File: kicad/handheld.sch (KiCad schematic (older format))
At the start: 23 parts, among them J1 Conn_01x08, J2 61300311121, J3 AVR-PDI-6, SW1 HOLD, SW2 PAUSE, SW3 SDROP, SW4 HDROP, SW5 ROTR, SW6 RIGHT, SW7 ROTL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

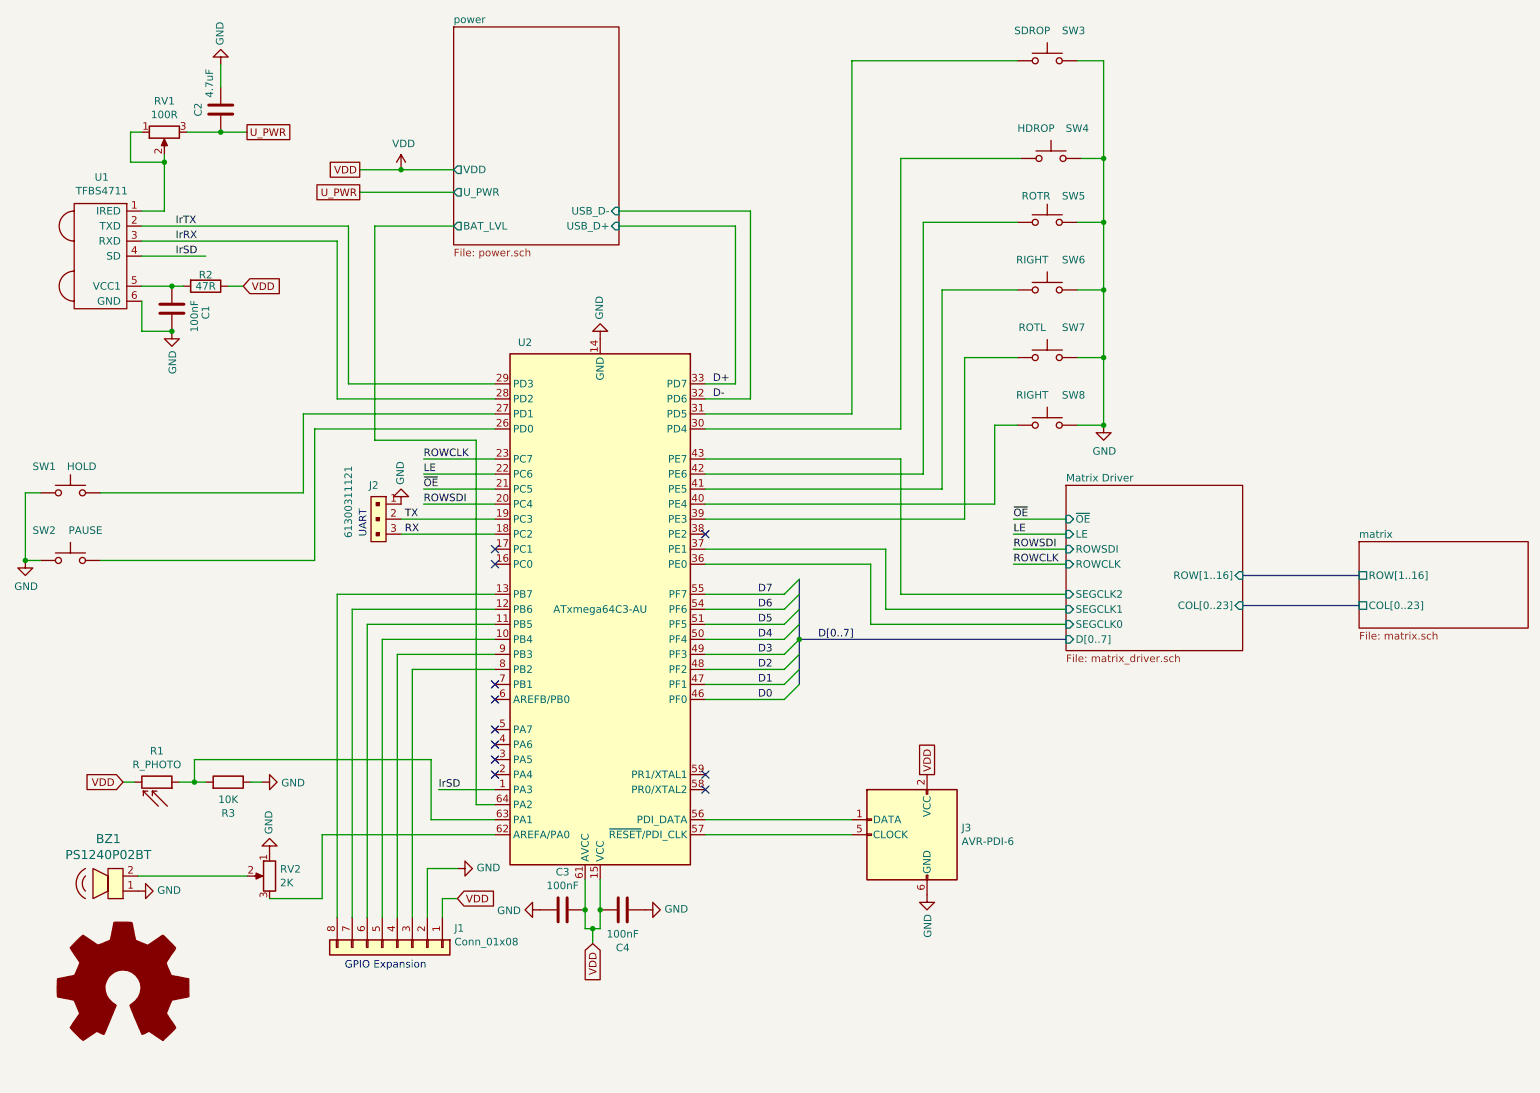
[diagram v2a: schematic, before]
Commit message: Decouple microcontroller
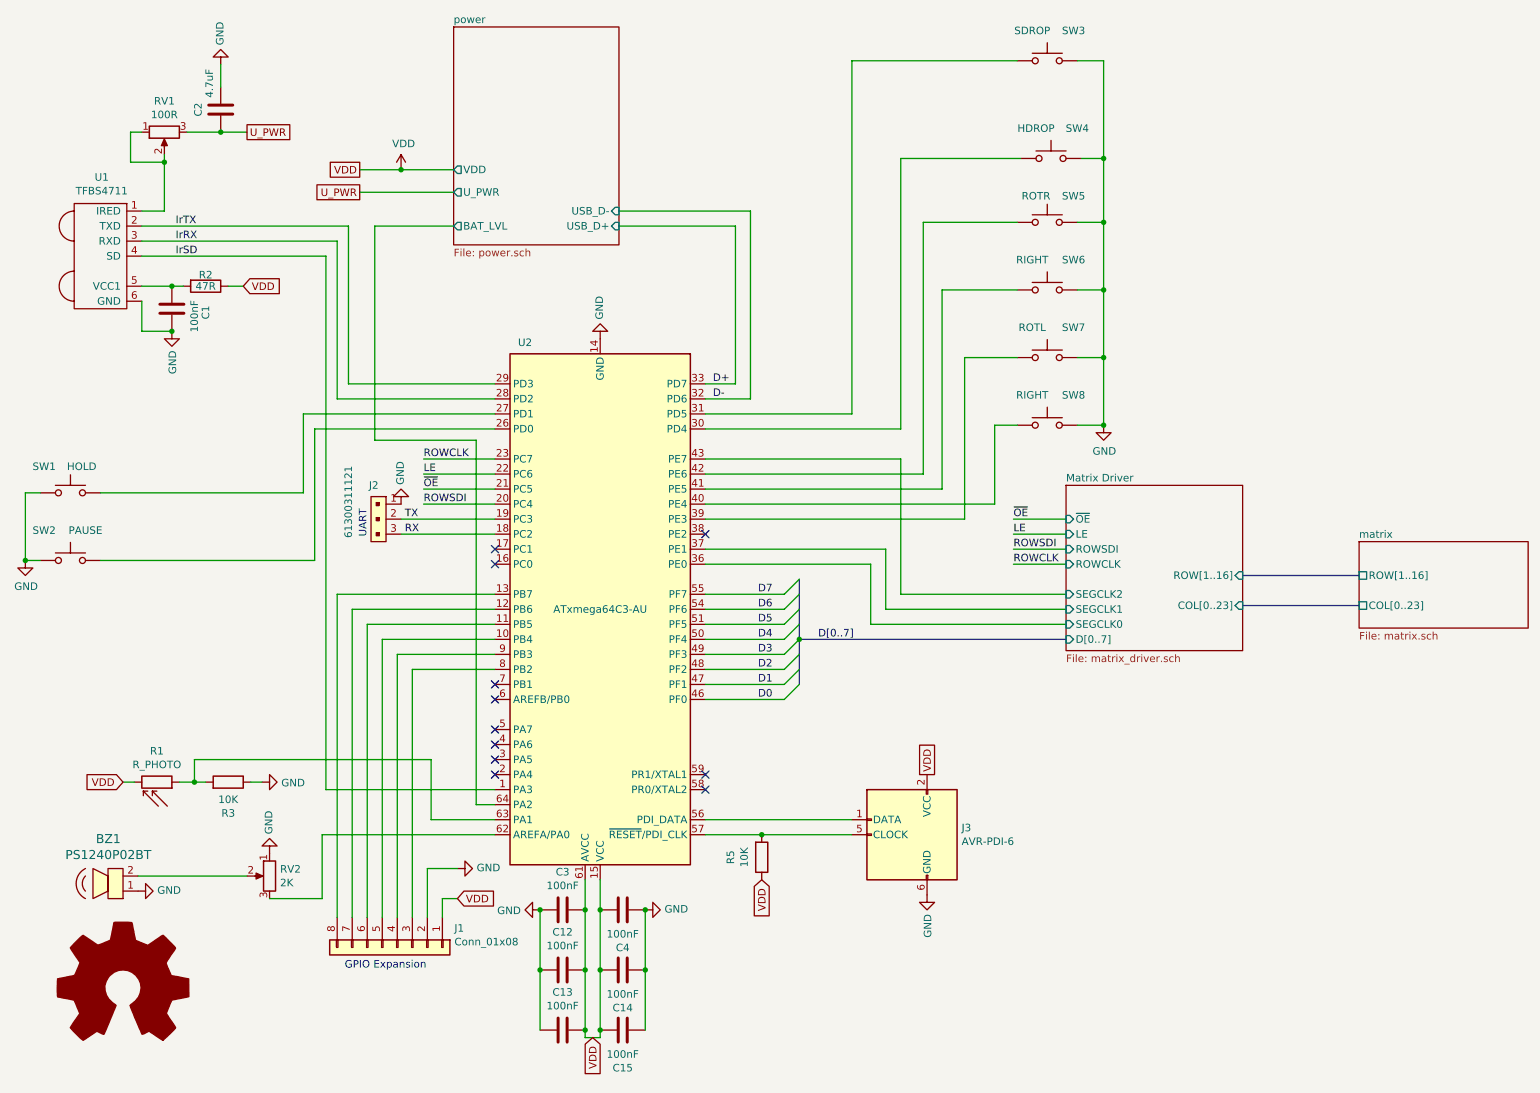
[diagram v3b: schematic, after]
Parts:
- added C12, C13, C14, C15: 100nF, Capacitor_SMD:C_0805_2012Metric_Pad1.15x1.40mm_HandSolder, symbol Device:C
- added R5: 10K, Resistor_SMD:R_0805_2012Metric_Pad1.15x1.40mm_HandSolder, symbol Device:R
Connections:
- net GND: now also C12.2, C13.2, C14.2, C15.2
- net VDD: now also C12.1, C13.1, C14.1, C15.1, R5.1
- net at J3.5 (CLOCK), U2.57 (~RESET~/PDI_CLK): now also R5.2
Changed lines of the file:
@@
 	4350 6475 4350 6675
 Wire Wire Line
-	4350 6675 4350 6800
-Wire Wire Line
-	4450 6800 4450 6675
-Connection ~ 4350 6675
-Connection ~ 4450 6675
+	4450 7525 4450 7475
 $Comp
 L Connector:AVR-PDI-6 J3
@@
 $EndComp
 Wire Wire Line
-	6125 6175 5150 6175
+	6125 6175 5525 6175
 Wire Wire Line
 	5150 6075 6125 6075
@@
 Wire Wire Line
 	3125 1750 3475 1750
-Text GLabel 4400 6900 3    50   Input ~ 0
+Text GLabel 4400 7525 3    50   Input ~ 0
 VDD
-Wire Wire Line
-	4350 6800 4400 6800
-Wire Wire Line
-	4400 6800 4400 6900
-Connection ~ 4400 6800
-Wire Wire Line
-	4400 6800 4450 6800
 Text GLabel 6625 5775 1    50   UnSpc ~ 0
 VDD
@@
 Wire Wire Line
 	2775 3175 3750 3175
-Wire Wire Line
-	3750 5875 3375 5875
-Text Label 3375 5875 0    50   ~ 0
-IrSD
 Text Label 1625 2325 0    50   ~ 0
 IrSD
-Wire Wire Line
-	1400 2325 1825 2325
 NoConn ~ 3750 4375
 NoConn ~ 3750 5475
@@
 	3200 5075 3200 6725
 NoConn ~ 3750 5175
+Wire Wire Line
+	4350 6675 4350 7075
+Connection ~ 4350 6675
+Connection ~ 4450 6675
+$Comp
+L Device:C C12
+U 1 1 5FD69EC0
+P 4200 7075
+F 0 "C12" V 3948 7075 50  0000 C CNN
+F 1 "100nF" V 4039 7075 50  0000 C CNN
+F 2 "Capacitor_SMD:C_0805_2012Metric_Pad1.15x1.40mm_HandSolder" H 4238 6925 50  0001 C CNN
+F 3 "~" H 4200 7075 50  0001 C CNN
+	1    4200 7075
+	0    1    1    0
+$EndComp
+Connection ~ 4350 7075
+Wire Wire Line
+	4350 7075 4350 7475
+$Comp
+L Device:C C14
+U 1 1 5FD6AC2B
+P 4600 7075
+F 0 "C14" V 4348 7075 50  0000 C CNN
+F 1 "100nF" V 4439 7075 50  0000 C CNN
+F 2 "Capacitor_SMD:C_0805_2012Metric_Pad1.15x1.40mm_HandSolder" H 4638 6925 50  0001 C CNN
+F 3 "~" H 4600 7075 50  0001 C CNN
+	1    4600 7075
+	0    -1   -1   0
+$EndComp
+Connection ~ 4450 7075
+Wire Wire Line
+	4450 7075 4450 6675
+$Comp
+L Device:C C13
+U 1 1 5FD6B34C
+P 4200 7475
+F 0 "C13" V 3948 7475 50  0000 C CNN
+F 1 "100nF" V 4039 7475 50  0000 C CNN
+F 2 "Capacitor_SMD:C_0805_2012Metric_Pad1.15x1.40mm_HandSolder" H 4238 7325 50  0001 C CNN
+F 3 "~" H 4200 7475 50  0001 C CNN
+	1    4200 7475
+	0    1    1    0
+$EndComp
+Connection ~ 4350 7475
+Wire Wire Line
+	4350 7475 4350 7525
+Wire Wire Line
+	4050 7475 4050 7075
+Connection ~ 4050 6675
+Connection ~ 4050 7075
+Wire Wire Line
+	4050 7075 4050 6675
+Wire Wire Line
+	4750 7075 4750 6675
+Connection ~ 4750 6675
+$Comp
+L Device:R R5
+U 1 1 5FD78AC8
+P 5525 6325
+F 0 "R5" V 5318 6325 50  0000 C CNN
+F 1 "10K" V 5409 6325 50  0000 C CNN
+F 2 "Resistor_SMD:R_0805_2012Metric_Pad1.15x1.40mm_HandSolder" V 5455 6325 50  0001 C CNN
+F 3 "~" H 5525 6325 50  0001 C CNN
+	1    5525 6325
+	1    0    0    1
+$EndComp
+Connection ~ 5525 6175
+Wire Wire Line
+	5525 6175 5150 6175
+Text GLabel 5525 6475 3    50   Input ~ 0
+VDD
+Wire Wire Line
+	4350 7525 4450 7525
+$Comp
+L Device:C C15
+U 1 1 5FDA21B7
+P 4600 7475
+F 0 "C15" V 4348 7475 50  0000 C CNN
+F 1 "100nF" V 4439 7475 50  0000 C CNN
+F 2 "Capacitor_SMD:C_0805_2012Metric_Pad1.15x1.40mm_HandSolder" H 4638 7325 50  0001 C CNN
+F 3 "~" H 4600 7475 50  0001 C CNN
+	1    4600 7475
+	0    -1   -1   0
+$EndComp
+Connection ~ 4450 7475
+Wire Wire Line
+	4450 7475 4450 7075
+Wire Wire Line
+	4750 7075 4750 7475
+Connection ~ 4750 7075
+Wire Wire Line
+	2625 2325 2625 5875
+Wire Wire Line
+	2625 5875 3750 5875
+Wire Wire Line
+	1400 2325 2625 2325
 Wire Bus Line
 	5775 4875 5775 5175

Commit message: Adds SELECT button
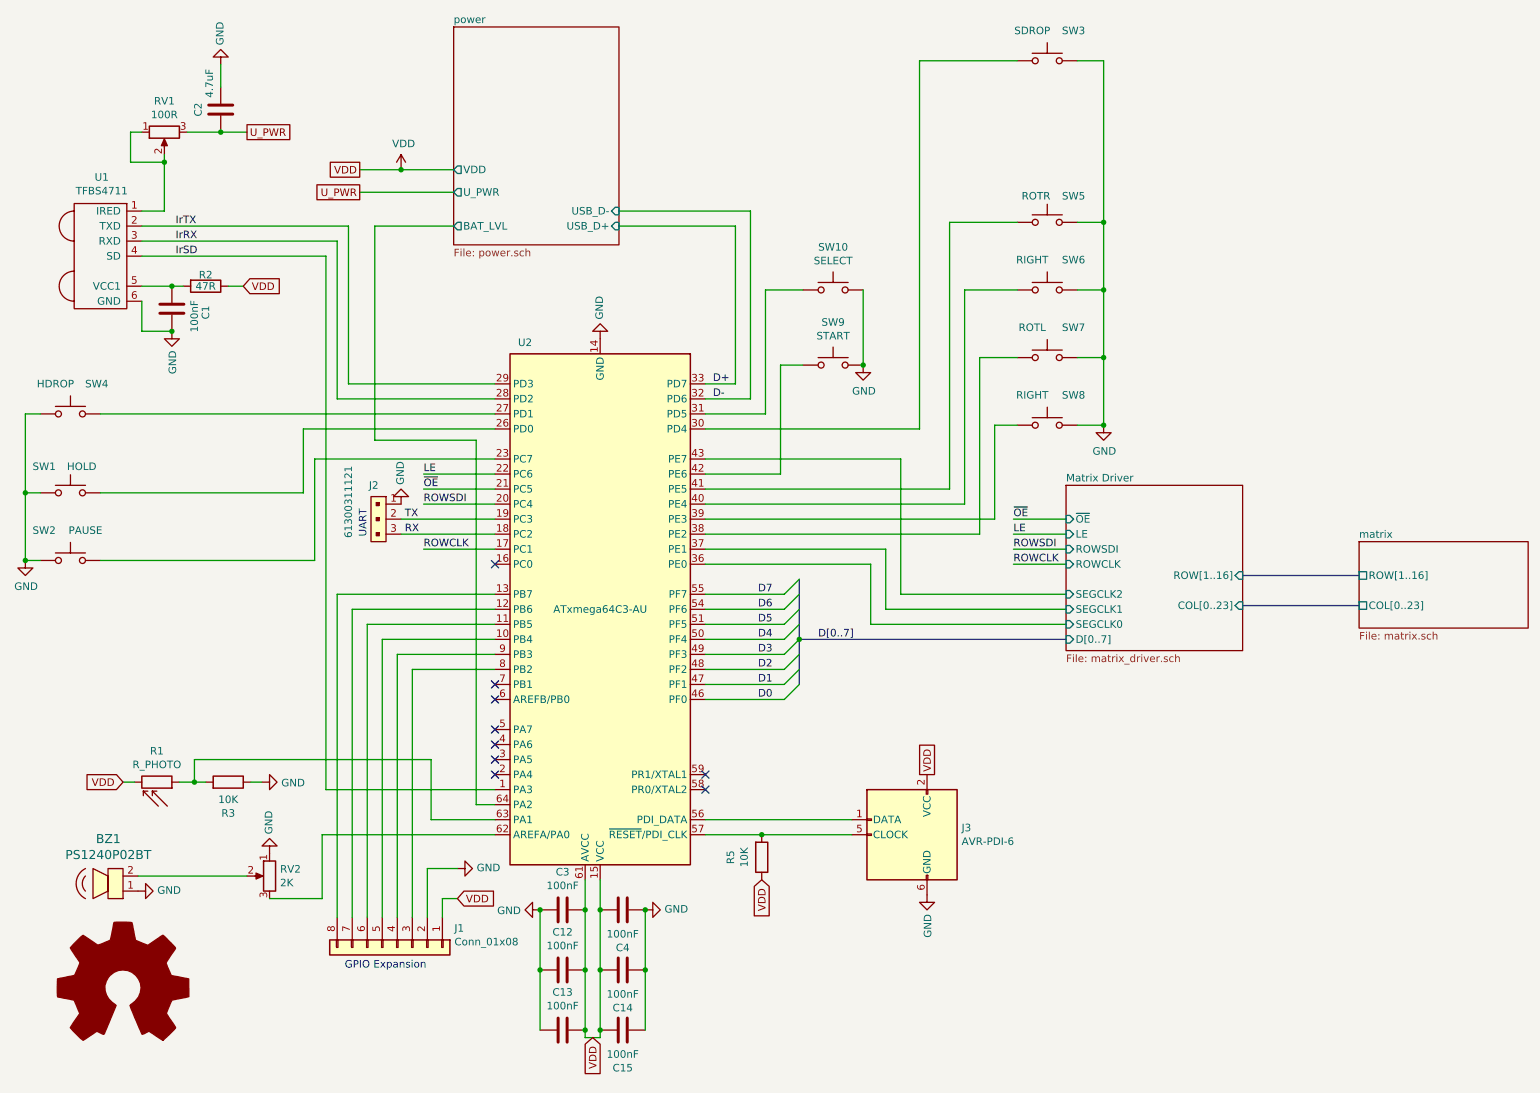
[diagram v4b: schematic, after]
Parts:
- added SW10: SELECT, Button_Switch_THT:SW_PUSH_6mm, symbol Switch:SW_Push
- added SW9: START, Button_Switch_THT:SW_PUSH_6mm, symbol Switch:SW_Push
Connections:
- net GND: now also SW4.2, SW10.2, SW9.2; no longer SW4.1
- net ROWCLK: now also U2.17 (PC1); no longer U2.23 (PC7)
- net at U2.30 (PD4): now also SW3.2; no longer SW4.2
- net at U2.31 (PD5): now also SW10.1; no longer SW3.2
- net at SW2.2: now also U2.23 (PC7); no longer U2.26 (PD0)
- net at U2.27 (PD1): now also SW4.1; no longer SW1.2
- net at SW8.2: now also U2.39 (PE3); no longer U2.40 (PE4)
- net at SW7.2: now also U2.38 (PE2); no longer U2.39 (PE3)
- net at SW6.2: now also U2.40 (PE4); no longer U2.41 (PE5)
- net at SW5.2: now also U2.41 (PE5); no longer U2.42 (PE6)
- new net: SW1.2, U2.26 (PD0)
- new net: SW9.1, U2.42 (PE6)
- no-connect marks 11 -> 9
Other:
- moved on the sheet: SW4
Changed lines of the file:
@@
 Wire Wire Line
 	1925 1500 2100 1500
-NoConn ~ 3750 4275
 Wire Wire Line
 	3625 3550 3625 5975
@@
 	3275 3875 3750 3875
 Wire Wire Line
-	3275 3675 3750 3675
+	3275 4275 3750 4275
 Wire Wire Line
 	3275 3775 3750 3775
@@
 L Switch:SW_Push SW4
 U 1 1 5FBDC4D1
-P 7450 1675
-F 0 "SW4" H 7275 1875 50  0000 C CNN
-F 1 "HDROP" H 7550 1875 50  0000 C CNN
-F 2 "Button_Switch_THT:SW_PUSH-12mm" H 7450 1875 50  0001 C CNN
-F 3 "~" H 7450 1875 50  0001 C CNN
-	1    7450 1675
+P 925 3375
+F 0 "SW4" H 750 3575 50  0000 C CNN
+F 1 "HDROP" H 1025 3575 50  0000 C CNN
+F 2 "Button_Switch_THT:SW_PUSH-12mm" H 925 3575 50  0001 C CNN
+F 3 "~" H 925 3575 50  0001 C CNN
+	1    925  3375
 	-1   0    0    -1
 $EndComp
@@
 	6350 4275 5150 4275
 Wire Wire Line
-	6450 4575 6450 3675
-Wire Wire Line
-	6450 3675 5150 3675
-Wire Wire Line
-	7225 2100 6600 2100
-Wire Wire Line
-	6600 2100 6600 3775
-Wire Wire Line
-	7225 2550 6725 2550
-Wire Wire Line
-	6725 2550 6725 3875
-Wire Wire Line
-	5150 3775 6600 3775
-Wire Wire Line
-	5150 3875 6725 3875
+	7225 2100 6775 2100
+Wire Wire Line
+	7225 2550 6875 2550
 Wire Wire Line
 	7225 3450 7075 3450
 Wire Wire Line
-	7075 3450 7075 3975
-Wire Wire Line
-	7075 3975 5150 3975
-Wire Wire Line
-	7225 3000 6875 3000
-Wire Wire Line
-	6875 3000 6875 4075
-Wire Wire Line
-	6875 4075 5150 4075
+	7225 3000 6975 3000
 Wire Wire Line
 	7625 3450 7800 3450
@@
 $EndComp
 Connection ~ 7800 3450
-NoConn ~ 5150 4175
 Text Label 3275 3975 0    50   ~ 0
 ROWSDI
@@
 Text Label 3275 3775 0    50   ~ 0
 LE
-Text Label 3275 3675 0    50   ~ 0
+Text Label 3275 4275 0    50   ~ 0
 ROWCLK
 Text Label 1625 2125 0    50   ~ 0
@@
 IrRX
 Wire Wire Line
-	5150 3375 6125 3375
-Wire Wire Line
-	6125 3375 6125 1025
-Wire Wire Line
-	6125 1025 7225 1025
+	6575 1025 7225 1025
 Wire Wire Line
 	7625 1025 7800 1025
-Wire Wire Line
-	7800 1025 7800 1675
 Connection ~ 7800 2100
 Wire Wire Line
-	5150 3475 6450 3475
-Wire Wire Line
-	6450 3475 6450 1675
-Wire Wire Line
-	6450 1675 7250 1675
-Wire Wire Line
-	7650 1675 7800 1675
-Connection ~ 7800 1675
-Wire Wire Line
-	7800 1675 7800 2100
-Wire Wire Line
-	2475 3900 2475 3375
-Wire Wire Line
-	2475 3375 3750 3375
-Wire Wire Line
-	3750 3475 2550 3475
-Wire Wire Line
-	2550 3475 2550 4350
+	1125 3375 3750 3375
 Wire Wire Line
 	1125 4350 2550 4350
@@
 Wire Wire Line
 	1400 2325 2625 2325
+Wire Wire Line
+	6975 4175 5150 4175
+Wire Wire Line
+	6975 3000 6975 4175
+Wire Wire Line
+	7075 4075 5150 4075
+Wire Wire Line
+	7075 3450 7075 4075
+Wire Wire Line
+	6875 3975 5150 3975
+Wire Wire Line
+	6875 2550 6875 3975
+Wire Wire Line
+	6775 3875 5150 3875
+Wire Wire Line
+	6775 2100 6775 3875
+Wire Wire Line
+	6450 3675 5150 3675
+Wire Wire Line
+	6450 3675 6450 4575
+$Comp
+L Switch:SW_Push SW9
+U 1 1 5FC778DC
+P 6000 3050
+F 0 "SW9" H 6000 3335 50  0000 C CNN
+F 1 "START" H 6000 3244 50  0000 C CNN
+F 2 "Button_Switch_THT:SW_PUSH_6mm" H 6000 3250 50  0001 C CNN
+F 3 "~" H 6000 3250 50  0001 C CNN
+	1    6000 3050
+	1    0    0    -1
+$EndComp
+$Comp
+L power:GND #PWR027
+U 1 1 5FC9EE66
+P 6200 3050
+F 0 "#PWR027" H 6200 2800 50  0001 C CNN
+F 1 "GND" H 6205 2877 50  0000 C CNN
+F 2 "" H 6200 3050 50  0001 C CNN
+F 3 "" H 6200 3050 50  0001 C CNN
+	1    6200 3050
+	1    0    0    -1
+$EndComp
+Wire Wire Line
+	5800 3050 5650 3050
+Wire Wire Line
+	5650 3050 5650 3775
+Wire Wire Line
+	5650 3775 5150 3775
+Wire Wire Line
+	2550 3675 3750 3675
+Wire Wire Line
+	2550 3675 2550 4350
+Wire Wire Line
+	2475 3475 3750 3475
+Wire Wire Line
+	2475 3475 2475 3900
+Wire Wire Line
+	7800 1025 7800 2100
+Wire Wire Line
+	725  3375 625  3375
+Wire Wire Line
+	625  3375 625  3900
+Connection ~ 625  3900
+Wire Wire Line
+	6575 1025 6575 3475
+Wire Wire Line
+	5150 3475 6575 3475
+$Comp
+L Switch:SW_Push SW10
+U 1 1 5FD1BDC4
+P 6000 2550
+F 0 "SW10" H 6000 2835 50  0000 C CNN
+F 1 "SELECT" H 6000 2744 50  0000 C CNN
+F 2 "Button_Switch_THT:SW_PUSH_6mm" H 6000 2750 50  0001 C CNN
+F 3 "~" H 6000 2750 50  0001 C CNN
+	1    6000 2550
+	1    0    0    -1
+$EndComp
+Wire Wire Line
+	6200 2550 6200 3050
+Connection ~ 6200 3050
+Wire Wire Line
+	5800 2550 5550 2550
+Wire Wire Line
+	5550 2550 5550 3375
+Wire Wire Line
+	5550 3375 5150 3375
 Wire Bus Line
 	5775 4875 5775 5175
